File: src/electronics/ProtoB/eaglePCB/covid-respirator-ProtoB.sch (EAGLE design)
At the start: 68 parts, among them IC1 AD825R, IC2 L7805CV-DG, IC3 AD8607R, IC4 AD8607R, T2 BC548

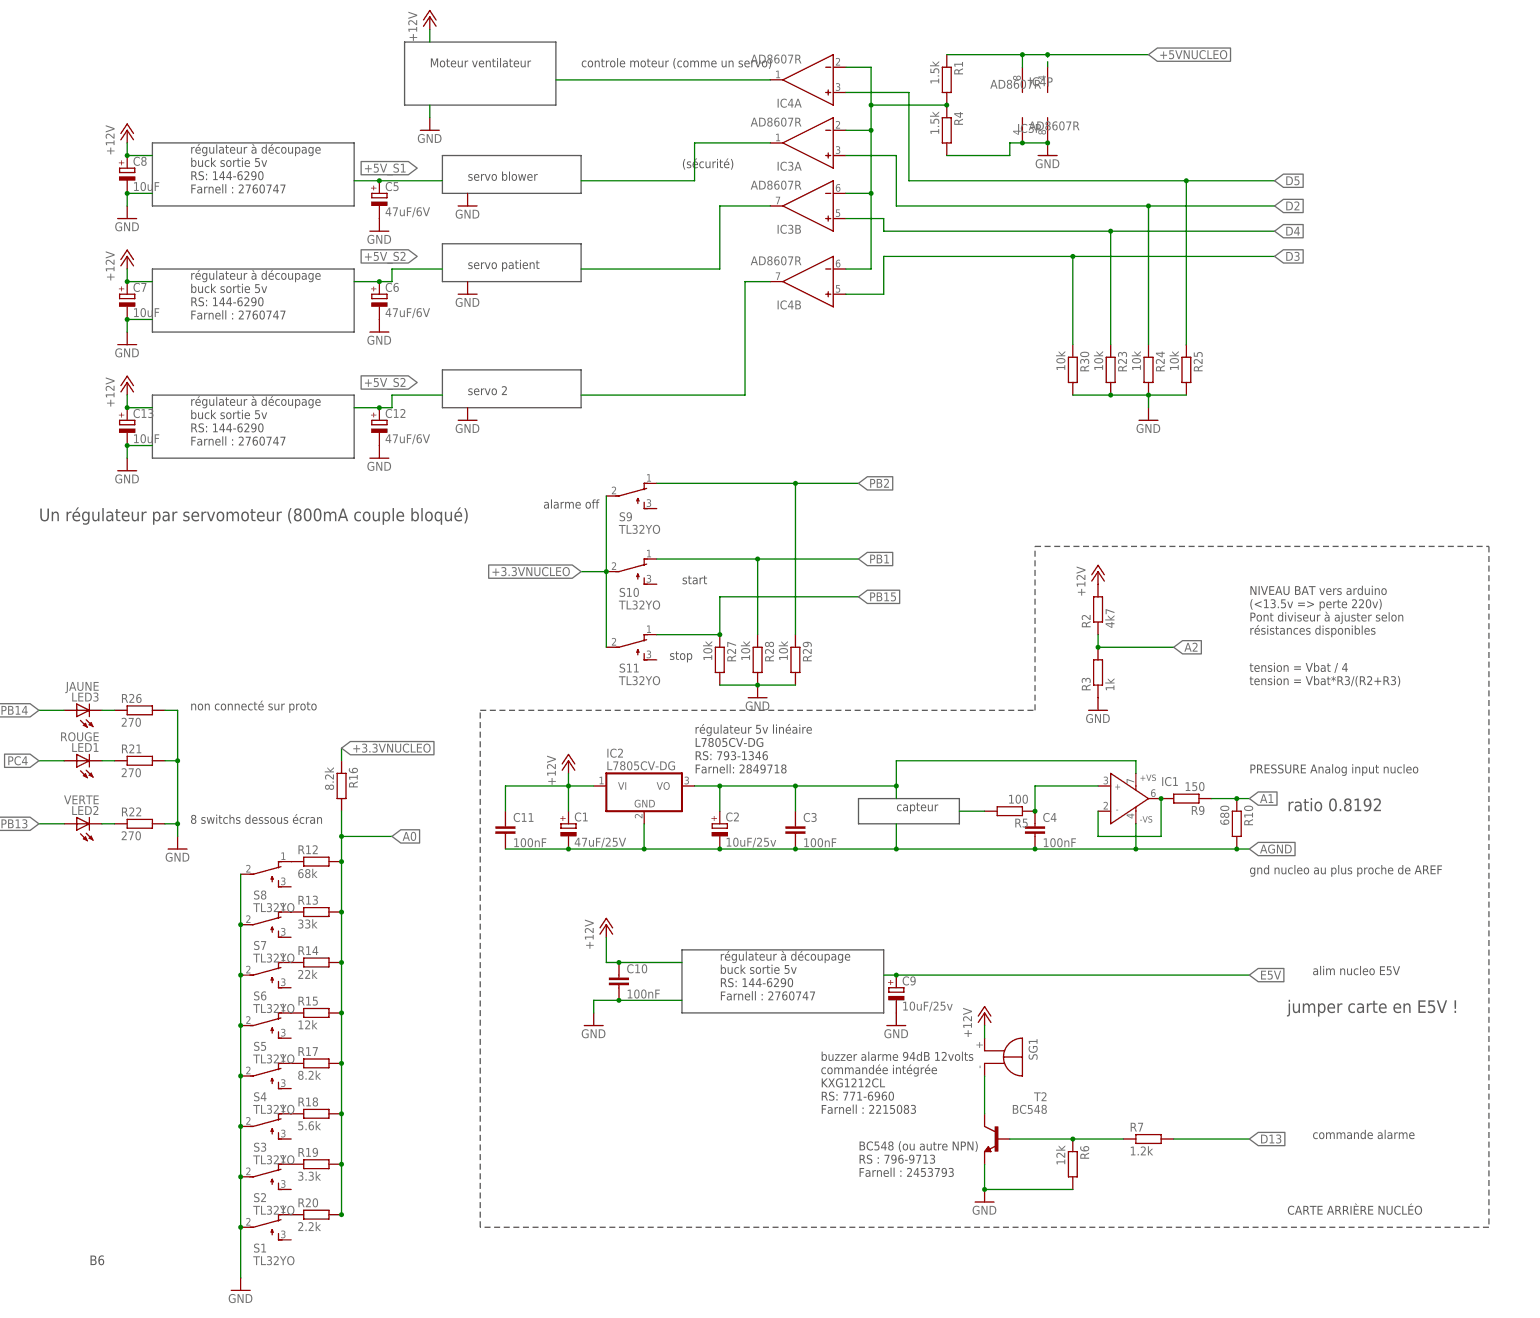
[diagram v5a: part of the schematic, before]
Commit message: change timer order to have timer3 for both servos
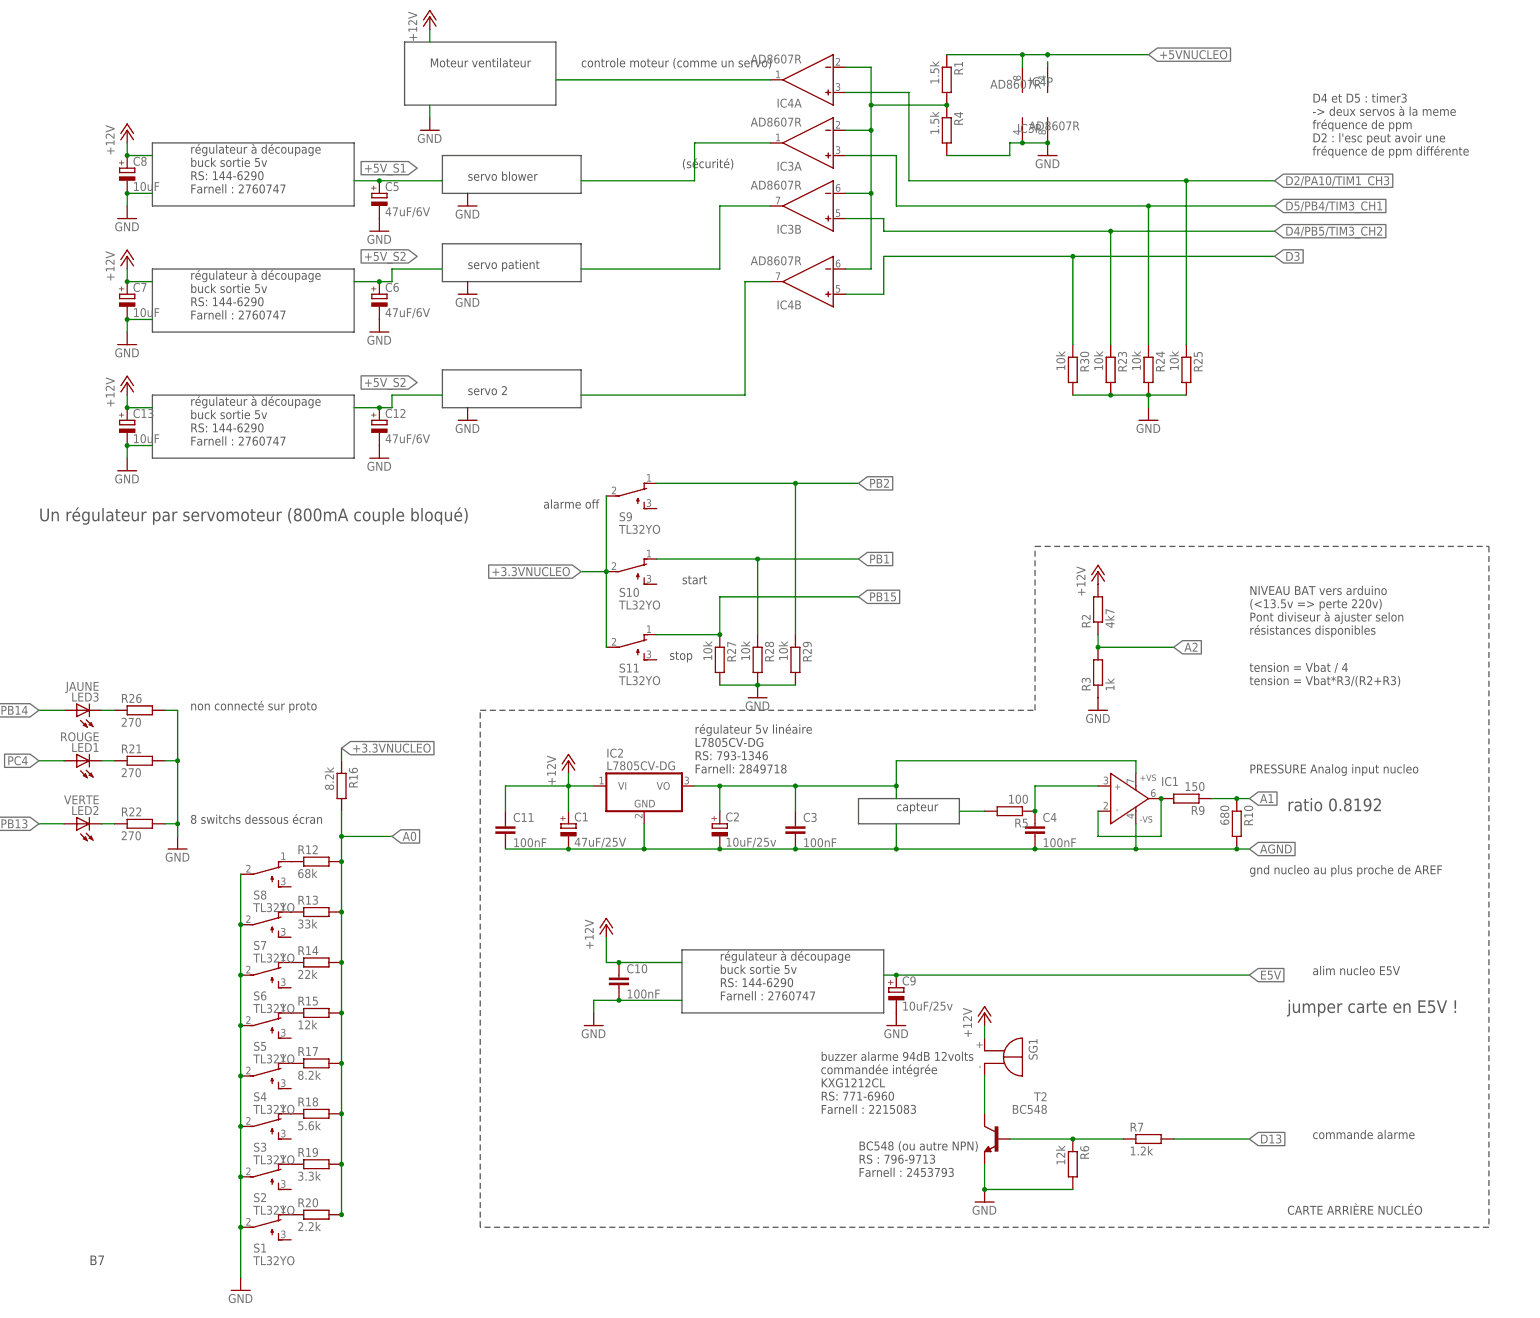
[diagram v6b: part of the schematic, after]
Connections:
- net D2 renamed D5/PB4/TIM3_CH1
- net D4 renamed D4/PB5/TIM3_CH2
- net D5 renamed D2/PA10/TIM1_CH3
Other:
- note added: "B7"
- note added: "D4 et D5 : timer3 -> deux servos à la meme fréquence de ppm D2 : l'esc peut avoir une fréquence de ppm différente"
- note removed: "B6"
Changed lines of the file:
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@@
 <text x="152.4" y="15.24" size="1.778" layer="97">start</text>
 <text x="149.86" y="0" size="1.778" layer="97">stop</text>
-<text x="33.02" y="-121.92" size="1.9304" layer="97">B6</text>
+<text x="33.02" y="-121.92" size="1.9304" layer="97">B7</text>
 <wire x1="45.72" y1="53.34" x2="86.36" y2="53.34" width="0.1524" layer="97"/>
 <wire x1="86.36" y1="53.34" x2="86.36" y2="40.64" width="0.1524" layer="97"/>
@@
 <wire x1="104.14" y1="50.8" x2="104.14" y2="58.42" width="0.1524" layer="97"/>
 <text x="109.22" y="53.34" size="1.778" layer="97">servo 2</text>
+<text x="279.4" y="101.6" size="1.778" layer="97">D4 et D5 : timer3
+-&gt; deux servos à la meme
+fréquence de ppm
+D2 : l'esc peut avoir une
+fréquence de ppm différente</text>
 </plain>
 <instances>
@@
 </segment>
 </net>
-<net name="D5" class="0">
-<segment>
-<pinref part="IC4" gate="A" pin="IN+"/>
-<wire x1="185.42" y1="114.3" x2="198.12" y2="114.3" width="0.1524" layer="91"/>
-<wire x1="198.12" y1="114.3" x2="198.12" y2="96.52" width="0.1524" layer="91"/>
-<wire x1="198.12" y1="96.52" x2="254" y2="96.52" width="0.1524" layer="91"/>
-<label x="271.78" y="96.52" size="1.778" layer="95" xref="yes"/>
-<pinref part="R25" gate="G$1" pin="1"/>
-<wire x1="254" y1="96.52" x2="271.78" y2="96.52" width="0.1524" layer="91"/>
-<wire x1="254" y1="63.5" x2="254" y2="96.52" width="0.1524" layer="91"/>
-<junction x="254" y="96.52"/>
-</segment>
-</net>
 <net name="A2" class="0">
 <segment>
@@
 </segment>
 </net>
-<net name="D2" class="0">
-<segment>
-<pinref part="IC3" gate="A" pin="IN+"/>
-<wire x1="185.42" y1="101.6" x2="195.58" y2="101.6" width="0.1524" layer="91"/>
-<wire x1="195.58" y1="101.6" x2="195.58" y2="91.44" width="0.1524" layer="91"/>
-<wire x1="195.58" y1="91.44" x2="246.38" y2="91.44" width="0.1524" layer="91"/>
-<label x="271.78" y="91.44" size="1.778" layer="95" xref="yes"/>
-<pinref part="R24" gate="G$1" pin="1"/>
-<wire x1="246.38" y1="91.44" x2="271.78" y2="91.44" width="0.1524" layer="91"/>
-<wire x1="246.38" y1="63.5" x2="246.38" y2="91.44" width="0.1524" layer="91"/>
-<junction x="246.38" y="91.44"/>
-</segment>
-</net>
-<net name="D4" class="0">
+<net name="D2/PA10/TIM1_CH3" class="0">
+<segment>
+<pinref part="IC4" gate="A" pin="IN+"/>
+<wire x1="185.42" y1="114.3" x2="198.12" y2="114.3" width="0.1524" layer="91"/>
+<wire x1="198.12" y1="114.3" x2="198.12" y2="96.52" width="0.1524" layer="91"/>
+<wire x1="198.12" y1="96.52" x2="254" y2="96.52" width="0.1524" layer="91"/>
+<label x="271.78" y="96.52" size="1.778" layer="95" xref="yes"/>
+<pinref part="R25" gate="G$1" pin="1"/>
+<wire x1="254" y1="96.52" x2="271.78" y2="96.52" width="0.1524" layer="91"/>
+<wire x1="254" y1="63.5" x2="254" y2="96.52" width="0.1524" layer="91"/>
+<junction x="254" y="96.52"/>
+</segment>
+</net>
+<net name="D4/PB5/TIM3_CH2" class="0">
 <segment>
 <pinref part="IC3" gate="B" pin="IN+"/>
@@
 </segment>
 </net>
+<net name="D5/PB4/TIM3_CH1" class="0">
+<segment>
+<pinref part="IC3" gate="A" pin="IN+"/>
+<wire x1="185.42" y1="101.6" x2="195.58" y2="101.6" width="0.1524" layer="91"/>
+<wire x1="195.58" y1="101.6" x2="195.58" y2="91.44" width="0.1524" layer="91"/>
+<wire x1="195.58" y1="91.44" x2="246.38" y2="91.44" width="0.1524" layer="91"/>
+<label x="271.78" y="91.44" size="1.778" layer="95" xref="yes"/>
+<pinref part="R24" gate="G$1" pin="1"/>
+<wire x1="246.38" y1="91.44" x2="271.78" y2="91.44" width="0.1524" layer="91"/>
+<wire x1="246.38" y1="63.5" x2="246.38" y2="91.44" width="0.1524" layer="91"/>
+<junction x="246.38" y="91.44"/>
+</segment>
+</net>
